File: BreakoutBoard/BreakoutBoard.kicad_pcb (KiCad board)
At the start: 2 copper layers, 43.2 x 55.9 mm, 7 parts, among them J1 addon_conn, J2 Power_top, J3 Power_bottom, J4 Conn_01x09, J5 Conn_01x10

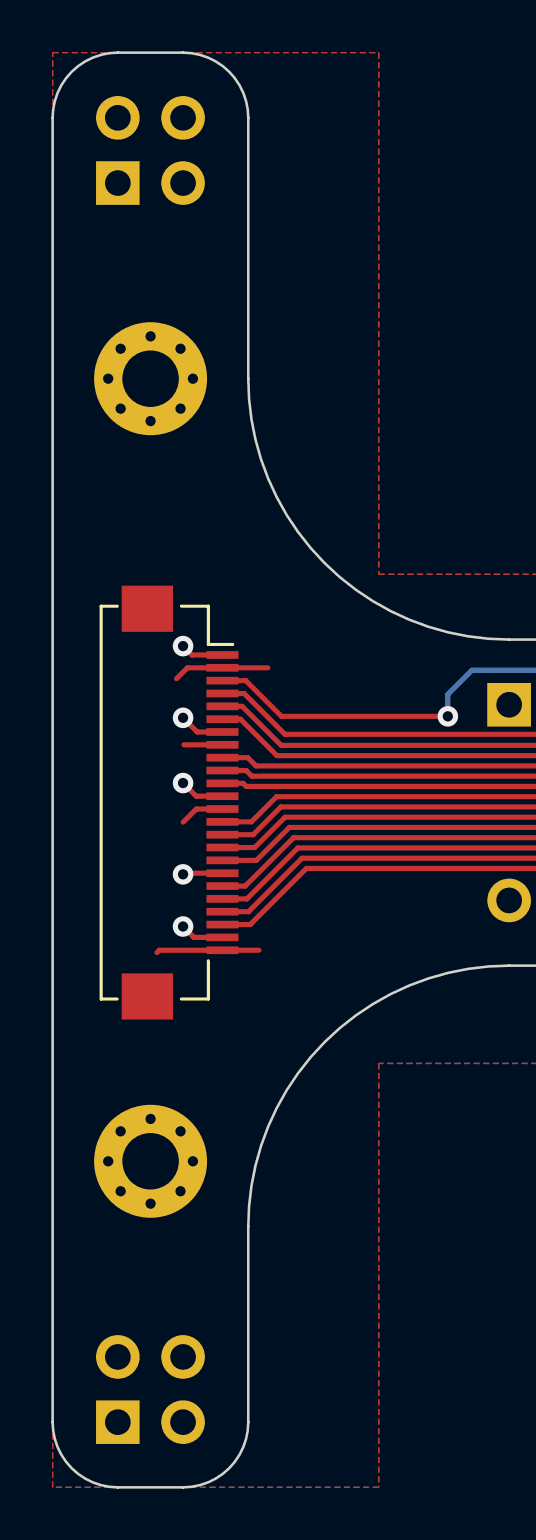
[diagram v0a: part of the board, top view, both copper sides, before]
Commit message: Rotates power pins on the breakout board
This will make the board sit on the left of the breadboard if the VCC
power rail is above the ground
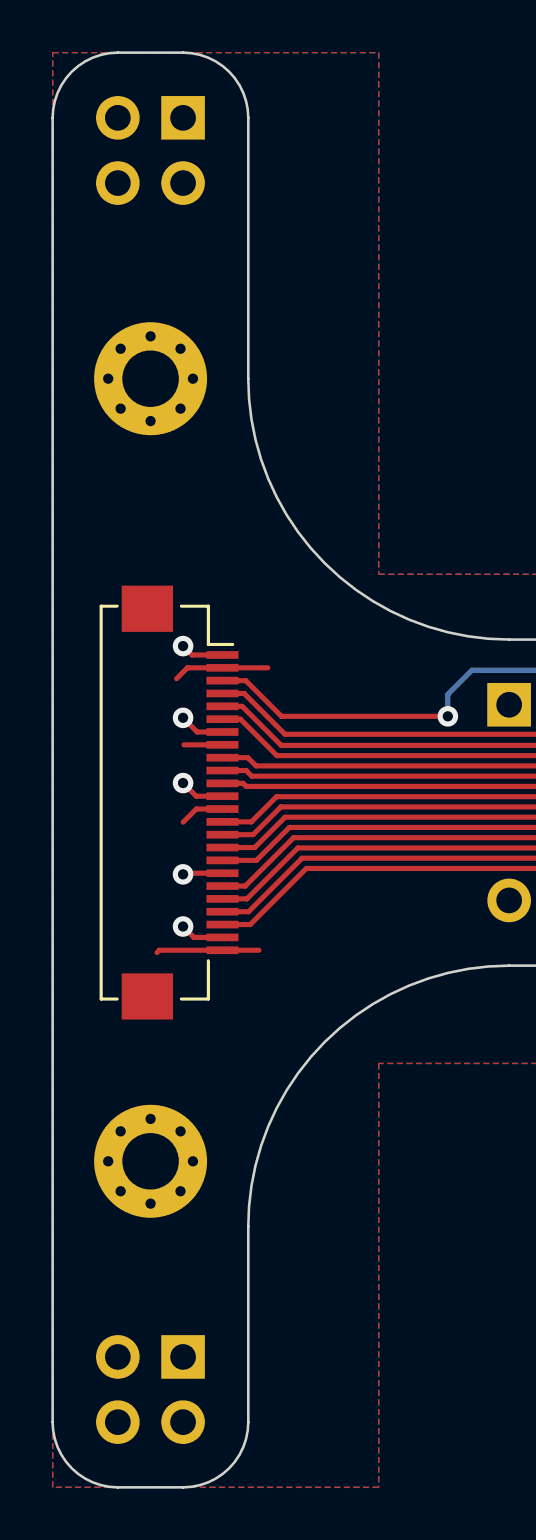
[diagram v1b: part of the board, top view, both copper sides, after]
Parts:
- moved J2 3.59 mm to (132.1, 73.7), turned to 180 degrees
- moved J3 3.59 mm to (132.1, 121.9), turned to 180 degrees
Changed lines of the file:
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@@
     )
   )
-  (footprint "Connector_PinHeader_2.54mm:PinHeader_2x02_P2.54mm_Vertical" locked (layer "B.Cu")
-    (at 129.54 76.2)
+  (footprint "Connector_PinHeader_2.54mm:PinHeader_2x02_P2.54mm_Vertical" (layer "B.Cu")
+    (at 132.08 73.66 180)
     (descr "Through hole straight pin header, 2x02, 2.54mm pitch, double rows")
     (tags "Through hole pin header THT 2x02 2.54mm double row")
@@
     (fp_line (start 3.81 1.27) (end 3.81 -3.81)
       (stroke (width 0.1) (type solid)) (layer "B.Fab"))
-    (pad "1" thru_hole rect locked (at 0 0) (size 1.7 1.7) (drill 1) (layers *.Cu *.Mask)
+    (pad "1" thru_hole rect locked (at 0 0 180) (size 1.7 1.7) (drill 1) (layers *.Cu *.Mask)
       (net 2 "+3V3") (pinfunction "Pin_1") (pintype "passive"))
-    (pad "2" thru_hole oval locked (at 2.54 0) (size 1.7 1.7) (drill 1) (layers *.Cu *.Mask)
+    (pad "2" thru_hole oval locked (at 2.54 0 180) (size 1.7 1.7) (drill 1) (layers *.Cu *.Mask)
       (net 2 "+3V3") (pinfunction "Pin_2") (pintype "passive"))
-    (pad "3" thru_hole oval locked (at 0 -2.54) (size 1.7 1.7) (drill 1) (layers *.Cu *.Mask)
+    (pad "3" thru_hole oval locked (at 0 -2.54 180) (size 1.7 1.7) (drill 1) (layers *.Cu *.Mask)
       (net 1 "GND") (pinfunction "Pin_3") (pintype "passive"))
-    (pad "4" thru_hole oval locked (at 2.54 -2.54) (size 1.7 1.7) (drill 1) (layers *.Cu *.Mask)
+    (pad "4" thru_hole oval locked (at 2.54 -2.54 180) (size 1.7 1.7) (drill 1) (layers *.Cu *.Mask)
       (net 1 "GND") (pinfunction "Pin_4") (pintype "passive"))
     (model "${KICAD6_3DMODEL_DIR}/Connector_PinHeader_2.54mm.3dshapes/PinHeader_2x02_P2.54mm_Vertical.wrl"
@@
     )
   )
-  (footprint "Connector_PinHeader_2.54mm:PinHeader_2x02_P2.54mm_Vertical" locked (layer "B.Cu")
-    (at 129.54 124.46)
+  (footprint "Connector_PinHeader_2.54mm:PinHeader_2x02_P2.54mm_Vertical" (layer "B.Cu")
+    (at 132.08 121.92 180)
     (descr "Through hole straight pin header, 2x02, 2.54mm pitch, double rows")
     (tags "Through hole pin header THT 2x02 2.54mm double row")
@@
     (fp_line (start 3.81 1.27) (end 3.81 -3.81)
       (stroke (width 0.1) (type solid)) (layer "B.Fab"))
-    (pad "1" thru_hole rect locked (at 0 0) (size 1.7 1.7) (drill 1) (layers *.Cu *.Mask)
+    (pad "1" thru_hole rect locked (at 0 0 180) (size 1.7 1.7) (drill 1) (layers *.Cu *.Mask)
       (net 2 "+3V3") (pinfunction "Pin_1") (pintype "passive"))
-    (pad "2" thru_hole oval locked (at 2.54 0) (size 1.7 1.7) (drill 1) (layers *.Cu *.Mask)
+    (pad "2" thru_hole oval locked (at 2.54 0 180) (size 1.7 1.7) (drill 1) (layers *.Cu *.Mask)
       (net 2 "+3V3") (pinfunction "Pin_2") (pintype "passive"))
-    (pad "3" thru_hole oval locked (at 0 -2.54) (size 1.7 1.7) (drill 1) (layers *.Cu *.Mask)
+    (pad "3" thru_hole oval locked (at 0 -2.54 180) (size 1.7 1.7) (drill 1) (layers *.Cu *.Mask)
       (net 1 "GND") (pinfunction "Pin_3") (pintype "passive"))
-    (pad "4" thru_hole oval locked (at 2.54 -2.54) (size 1.7 1.7) (drill 1) (layers *.Cu *.Mask)
+    (pad "4" thru_hole oval locked (at 2.54 -2.54 180) (size 1.7 1.7) (drill 1) (layers *.Cu *.Mask)
       (net 1 "GND") (pinfunction "Pin_4") (pintype "passive"))
     (model "${KICAD6_3DMODEL_DIR}/Connector_PinHeader_2.54mm.3dshapes/PinHeader_2x02_P2.54mm_Vertical.wrl"

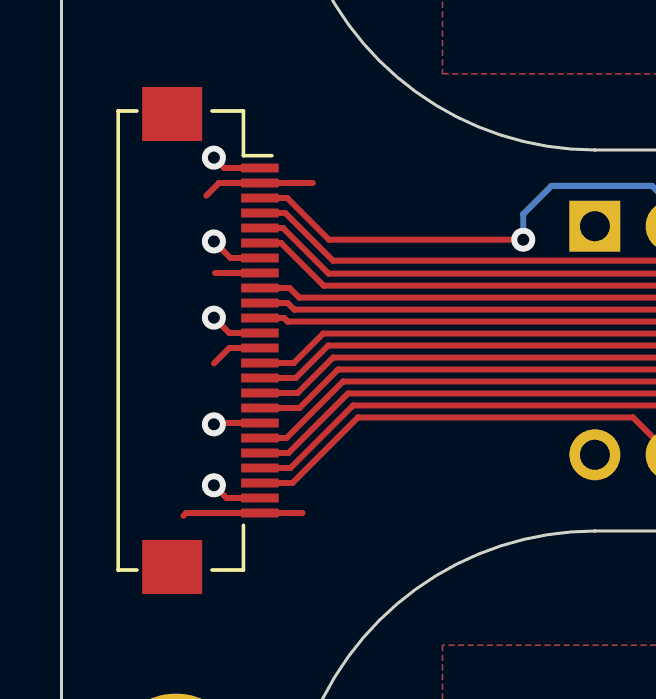
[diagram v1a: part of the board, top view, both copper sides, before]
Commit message: Fixes DRC warnings
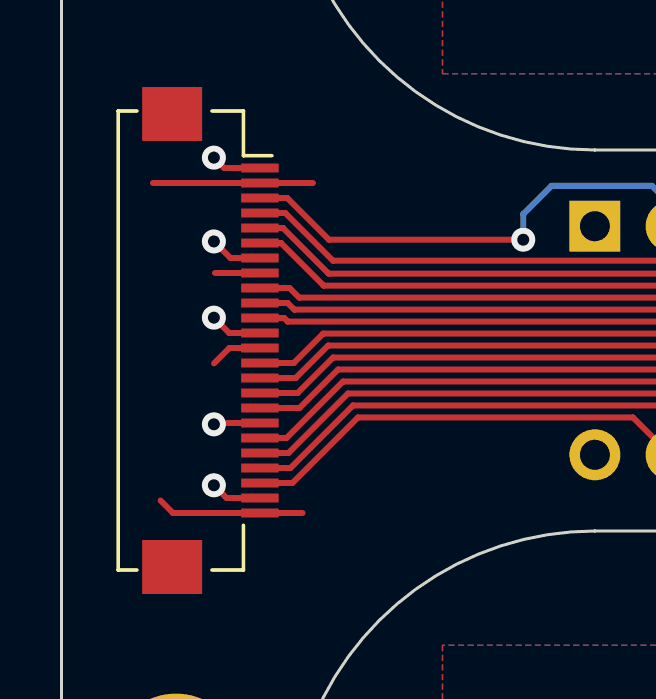
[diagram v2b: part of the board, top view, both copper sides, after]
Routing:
- net +3V3: track 11.0 -> 13.5 mm
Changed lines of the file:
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@@
   (segment (start 133.615 106.08) (end 131.156 106.08) (width 0.2) (layer "F.Cu") (net 2))
   (segment (start 133.615 106.08) (end 135.036 106.08) (width 0.2) (layer "F.Cu") (net 2))
-  (segment (start 133.615 95.08) (end 132.25 95.08) (width 0.2) (layer "F.Cu") (net 2))
+  (segment (start 131.156 106.08) (end 130.718 106.08) (width 0.2) (layer "F.Cu") (net 2))
+  (segment (start 133.615 95.08) (end 130.048 95.08) (width 0.2) (layer "F.Cu") (net 2))
   (segment (start 133.615 95.08) (end 135.382 95.08) (width 0.2) (layer "F.Cu") (net 2))
-  (segment (start 131.156 106.08) (end 131.064 106.172) (width 0.2) (layer "F.Cu") (net 2))
+  (segment (start 130.718 106.08) (end 130.302 105.664) (width 0.2) (layer "F.Cu") (net 2))
   (segment (start 132.596 100.58) (end 133.615 100.58) (width 0.2) (layer "F.Cu") (net 2))
   (segment (start 132.116 98.08) (end 133.615 98.08) (width 0.2) (layer "F.Cu") (net 2))
-  (segment (start 132.25 95.08) (end 131.826 95.504) (width 0.2) (layer "F.Cu") (net 2))
   (segment (start 132.084 101.092) (end 132.596 100.58) (width 0.2) (layer "F.Cu") (net 2))
   (segment (start 142.3924 96.970011) (end 135.914417 96.970011) (width 0.2) (layer "F.Cu") (net 3))

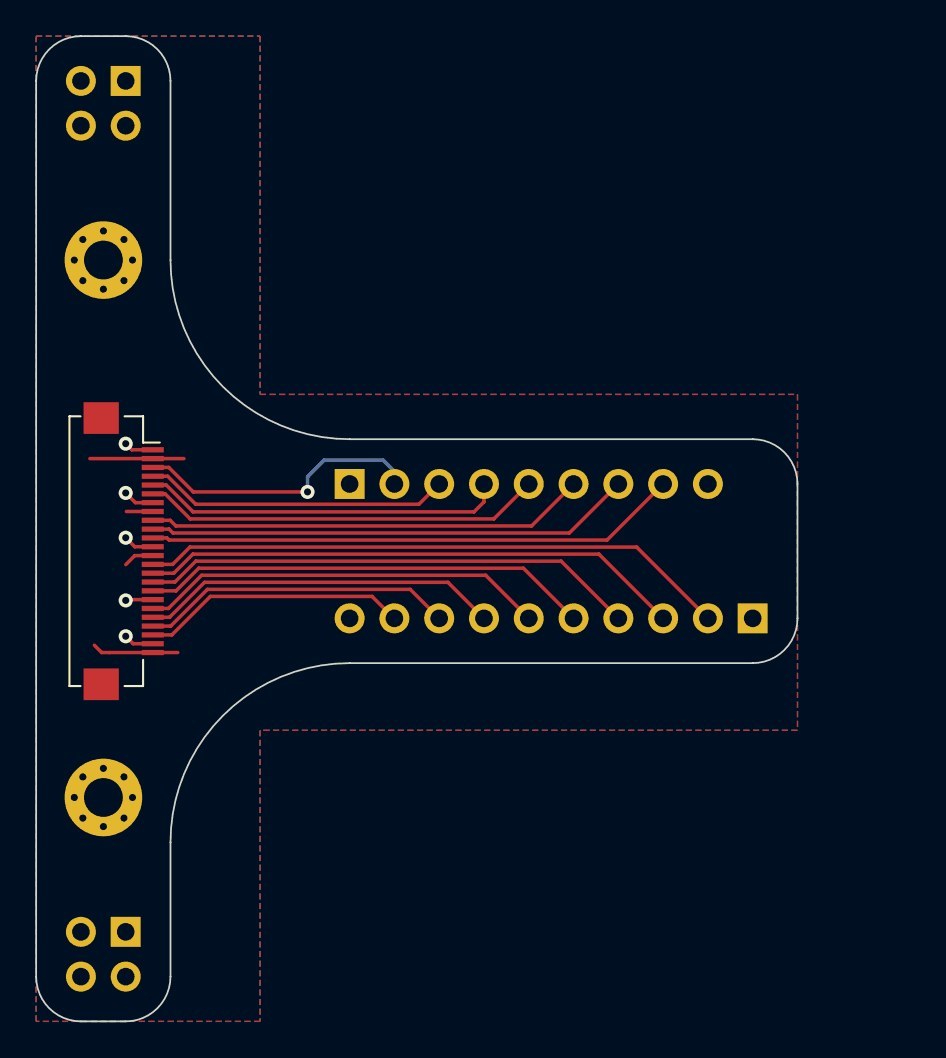
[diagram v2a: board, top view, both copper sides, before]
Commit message: Adds labels to broken out pins
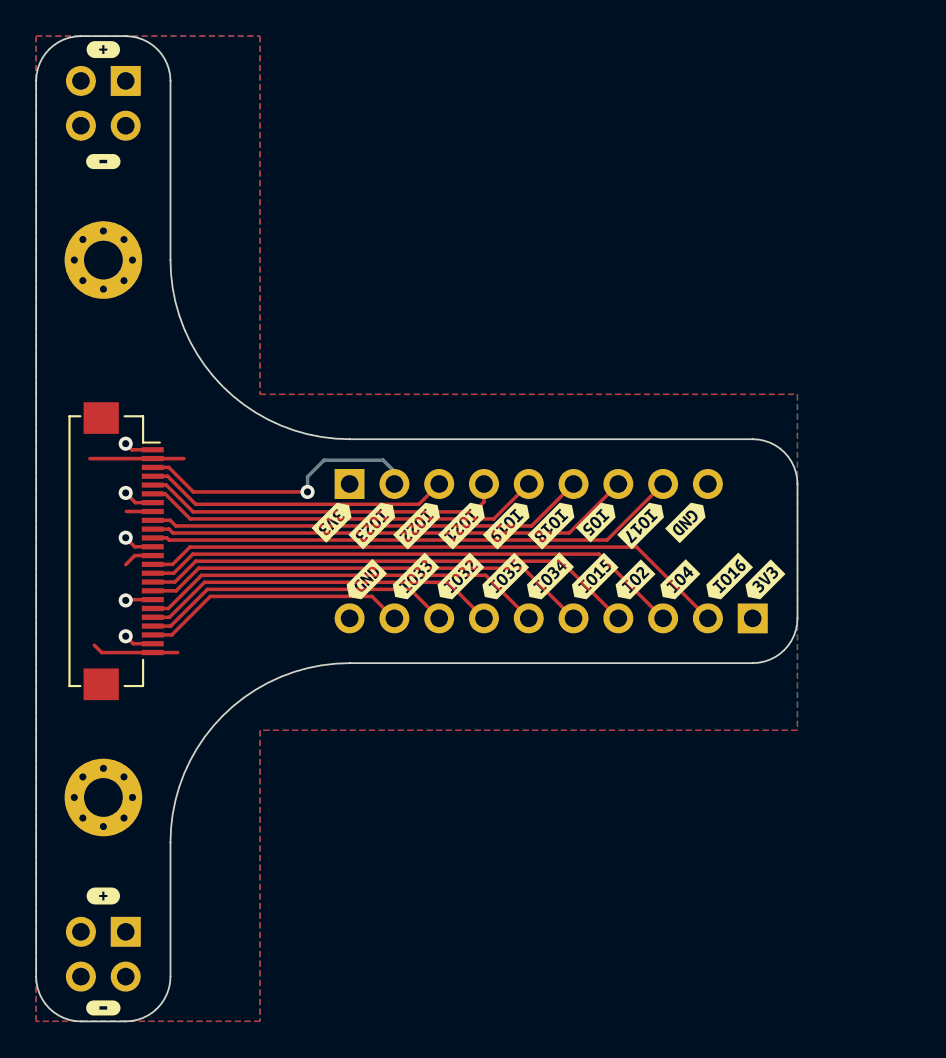
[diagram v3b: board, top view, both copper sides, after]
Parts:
- added kibuzzard-62594249: G***, kibuzzard-62594249, F.Cu at (130.8, 126.2)
- added kibuzzard-62594249: G***, kibuzzard-62594249, F.Cu at (130.8, 78.2)
- added kibuzzard-6259425C: G***, kibuzzard-6259425C, F.Cu at (130.8, 71.9)
- added kibuzzard-6259425C: G***, kibuzzard-6259425C, F.Cu at (130.8, 119.9)
- added kibuzzard-625944D4: G***, kibuzzard-625944D4, F.Cu at (153.8, 98.8)
- added kibuzzard-625944DF: G***, kibuzzard-625944DF, F.Cu at (151.3, 98.8)
- added kibuzzard-625944E4: G***, kibuzzard-625944E4, F.Cu at (148.7, 98.8)
- added kibuzzard-625944EE: G***, kibuzzard-625944EE, F.Cu at (146.2, 98.8)
- added kibuzzard-625944F4: G***, kibuzzard-625944F4, F.Cu at (143.9, 98.6)
- added kibuzzard-625944FA: G***, kibuzzard-625944FA, F.Cu at (156.3, 98.8)
- added kibuzzard-625944FF: G***, kibuzzard-625944FF, F.Cu at (158.9, 98.6)
- added kibuzzard-62594504: G***, kibuzzard-62594504, F.Cu at (161.4, 98.8)
- added kibuzzard-62594508: G***, kibuzzard-62594508, F.Cu at (164.0, 98.6)
- added kibuzzard-6259452C: G***, kibuzzard-6259452C, F.Cu at (145.6, 102.1)
- added kibuzzard-62594532: G***, kibuzzard-62594532, F.Cu at (148.4, 101.9)
- added kibuzzard-6259453A: G***, kibuzzard-6259453A, F.Cu at (151.0, 101.9)
- added kibuzzard-6259453E: G***, kibuzzard-6259453E, F.Cu at (153.5, 101.9)
- added kibuzzard-62594542: G***, kibuzzard-62594542, F.Cu at (156.0, 101.9)
- added kibuzzard-62594546: G***, kibuzzard-62594546, F.Cu at (158.6, 101.9)
- added kibuzzard-6259454A: G***, kibuzzard-6259454A, F.Cu at (160.9, 102.1)
- added kibuzzard-6259454F: G***, kibuzzard-6259454F, F.Cu at (163.4, 102.1)
- added kibuzzard-62594553: G***, kibuzzard-62594553, F.Cu at (166.2, 101.9)
- added kibuzzard-62594559: G***, kibuzzard-62594559, F.Cu at (168.2, 102.1)

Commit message: Fixes position of the power connectors on breakout board
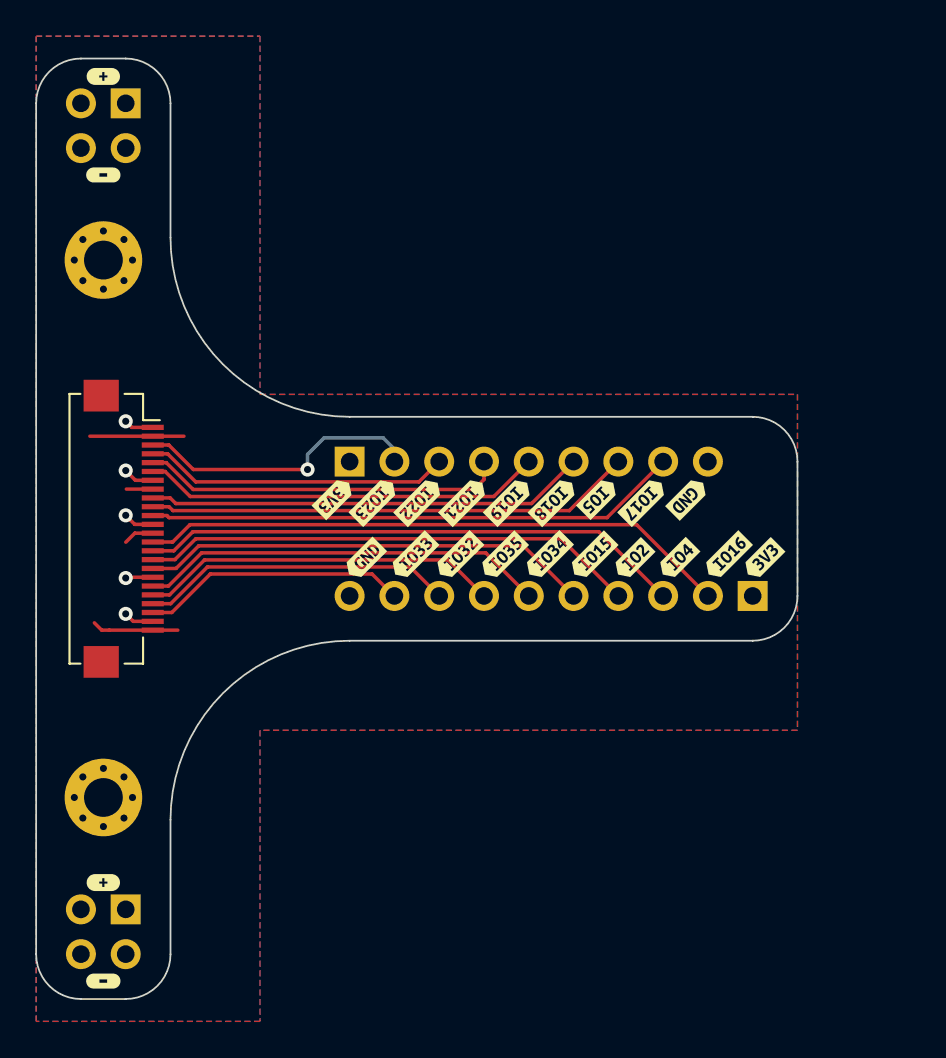
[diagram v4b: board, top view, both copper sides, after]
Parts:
- moved kibuzzard-62594249 1.52 mm to (130.8, 124.7)
- moved kibuzzard-6259425C 1.52 mm to (130.8, 73.4)
- moved J3 1.28 mm to (132.1, 120.6)
- moved J2 1.27 mm to (132.1, 74.9)
- moved kibuzzard-625944D4 1.27 mm to (153.8, 97.5)
- moved kibuzzard-625944EE 1.27 mm to (146.2, 97.5)
- moved kibuzzard-625944FF 1.27 mm to (158.9, 97.3)
- moved kibuzzard-62594532 1.27 mm to (148.4, 100.6)
- moved kibuzzard-6259453A 1.27 mm to (151.0, 100.6)
- moved kibuzzard-6259453E 1.27 mm to (153.5, 100.6)
- moved kibuzzard-62594546 1.27 mm to (158.6, 100.6)
- moved J1 1.27 mm to (131.8, 99.1)
- moved J4 1.27 mm to (144.8, 95.2)
- moved J5 1.27 mm to (167.6, 102.9)
- moved kibuzzard-625944DF 1.27 mm to (151.3, 97.5)
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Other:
- board size 43.2 x 55.9 mm -> 43.2 x 53.3 mm
